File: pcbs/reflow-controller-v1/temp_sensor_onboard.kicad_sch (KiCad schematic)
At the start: 4 parts, among them U1 TMP1075DSG, U2 TMP1075DSG

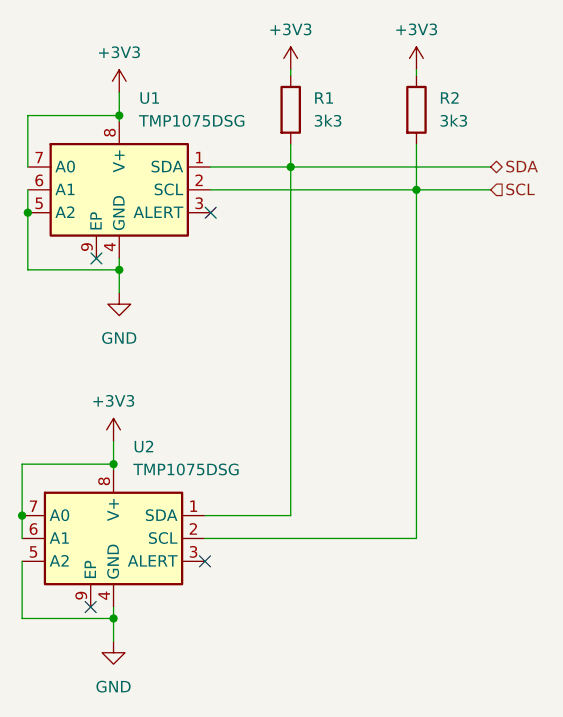
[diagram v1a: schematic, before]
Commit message: update hv placment&routing + add initiall hv lv seperation
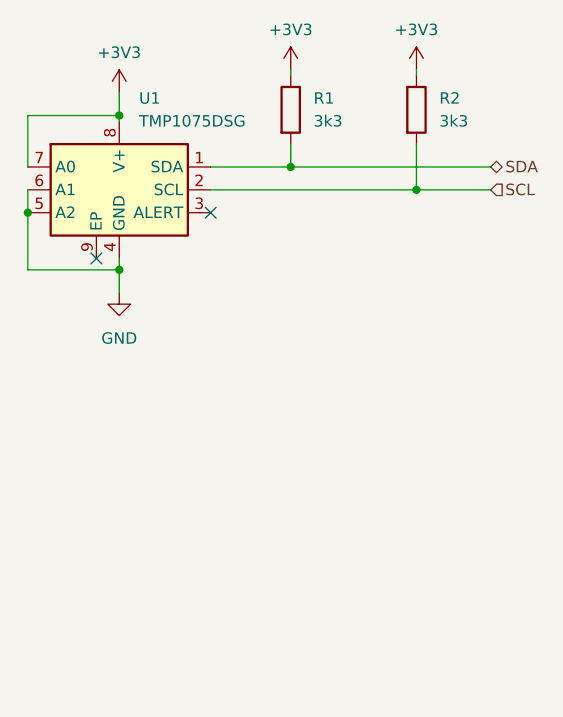
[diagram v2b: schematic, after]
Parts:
- removed U2: TMP1075DSG, Package_SON:WSON-8-1EP_2x2mm_P0.5mm_EP0.9x1.6mm, symbol Sensor_Temperature:TMP1075DSG
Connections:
- no-connect marks 4 -> 2

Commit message: update display placing & prelim. routing
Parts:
- U1: footprint Package_SON:WSON-8-1EP_2x2mm_P0.5mm_EP0.9x1.6mm -> Package_SON:WSON-8-1EP_2x2mm_P0.5mm_EP0.9x1.6mm_ThermalVias
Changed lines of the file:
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@@
 			)
 		)
-		(property "Description" ""
+		(property "Description" "Power symbol creates a global label with name \"+3V3\""
 			(at 160.02 75.565 0)
 			(effects
@@
 			)
 		)
-		(property "Description" ""
+		(property "Description" "Power symbol creates a global label with name \"+3V3\""
 			(at 173.99 75.565 0)
 			(effects
@@
 			)
 		)
-		(property "Description" ""
+		(property "Description" "Power symbol creates a global label with name \"GND\" , ground"
 			(at 140.97 100.33 0)
 			(effects
@@
 			)
 		)
-		(property "Description" ""
+		(property "Description" "Resistor"
 			(at 173.99 80.01 0)
 			(effects
@@
 			)
 		)
-		(property "Description" ""
+		(property "Description" "Resistor"
 			(at 160.02 80.01 0)
 			(effects
@@
 			)
 		)
-		(property "Footprint" "Package_SON:WSON-8-1EP_2x2mm_P0.5mm_EP0.9x1.6mm"
+		(property "Footprint" "Package_SON:WSON-8-1EP_2x2mm_P0.5mm_EP0.9x1.6mm_ThermalVias"
 			(at 142.875 95.25 0)
 			(effects
@@
 			)
 		)
-		(property "Description" ""
+		(property "Description" "I2C-bus digital temperature sensor and thermal watchdog, WSON-8"
 			(at 140.97 88.9 0)
 			(effects
@@
 			)
 		)
-		(property "Description" ""
+		(property "Description" "Power symbol creates a global label with name \"+3V3\""
 			(at 140.97 78.105 0)
 			(effects
